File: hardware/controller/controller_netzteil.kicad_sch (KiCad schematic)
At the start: 16 parts, among them J1 230V~, U1 IRM-10-5, U2 AP7361C-33E

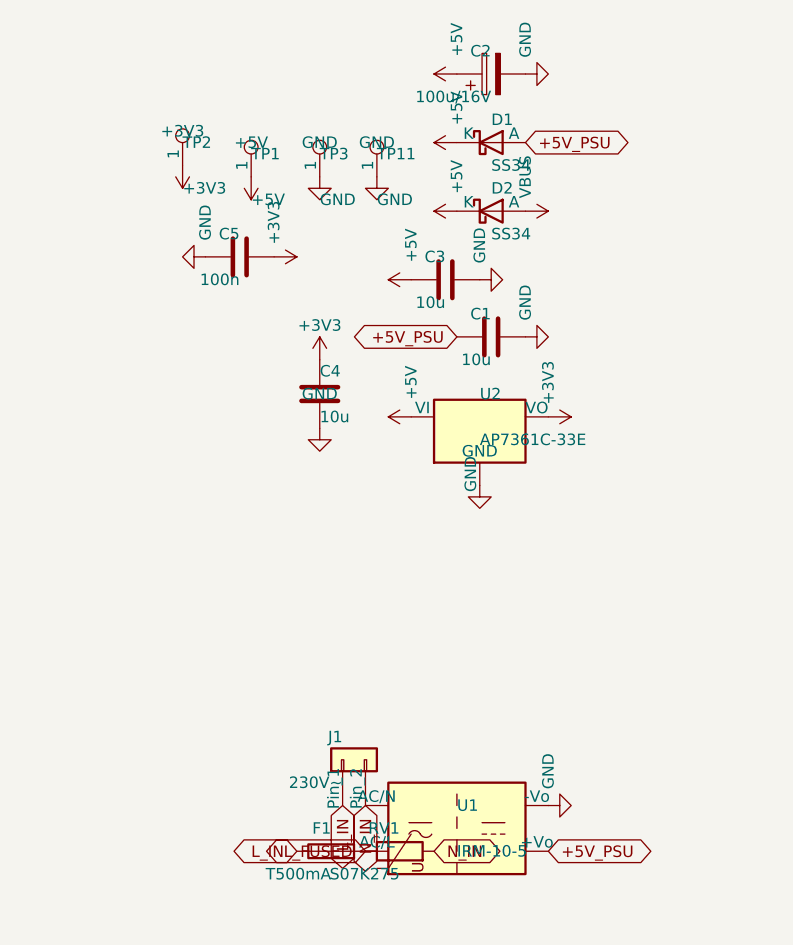
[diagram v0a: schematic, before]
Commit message: feat(hardware): MAX31856 input filter per datasheet, sheet cleanup in progress
- Input filter per MAX31856 "Typical Application Circuit": C14/C17 100 nF
  differential, new C27-C30 10 nF from T+/T- to GND; reference netlist re-exported
- Datasheet checks: BIAS to T- confirmed, FAULT is push-pull (diodes to CLR needed)
- check_schematic.py: sheet format check (raw newline in strings breaks KiCad)
- import_netlist.py: relinks by reference when a symbol gets a new UUID (U7 case)
- Sheets partly rearranged in KiCad by the user (connectivity unchanged, 0 errors)
- MAX31856 order number and price, docs/Component-Specs ignored

Co-Authored-By: Claude Opus 5.5 <noreply@anthropic.com>
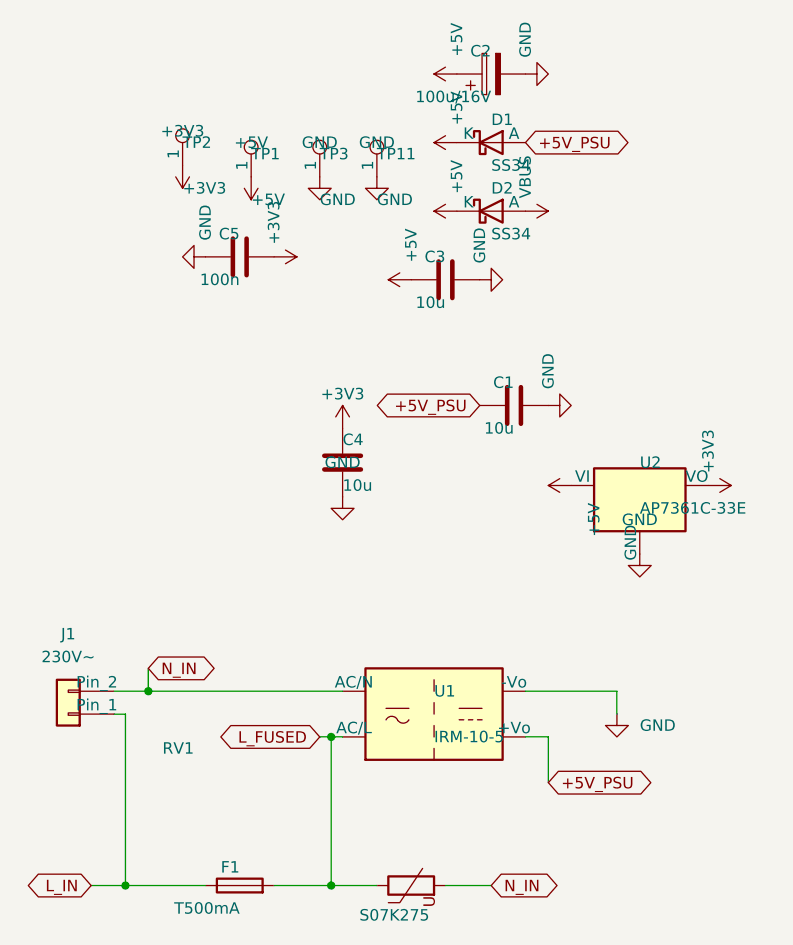
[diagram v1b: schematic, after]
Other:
- moved on the sheet: C1, C4, F1, J1, RV1, U1, U2
